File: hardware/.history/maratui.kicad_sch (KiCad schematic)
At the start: 5 parts, among them J1 Power Supply, J2 Lelit Mara, SW1 Button, U1 Ili9341_TFT_320x240

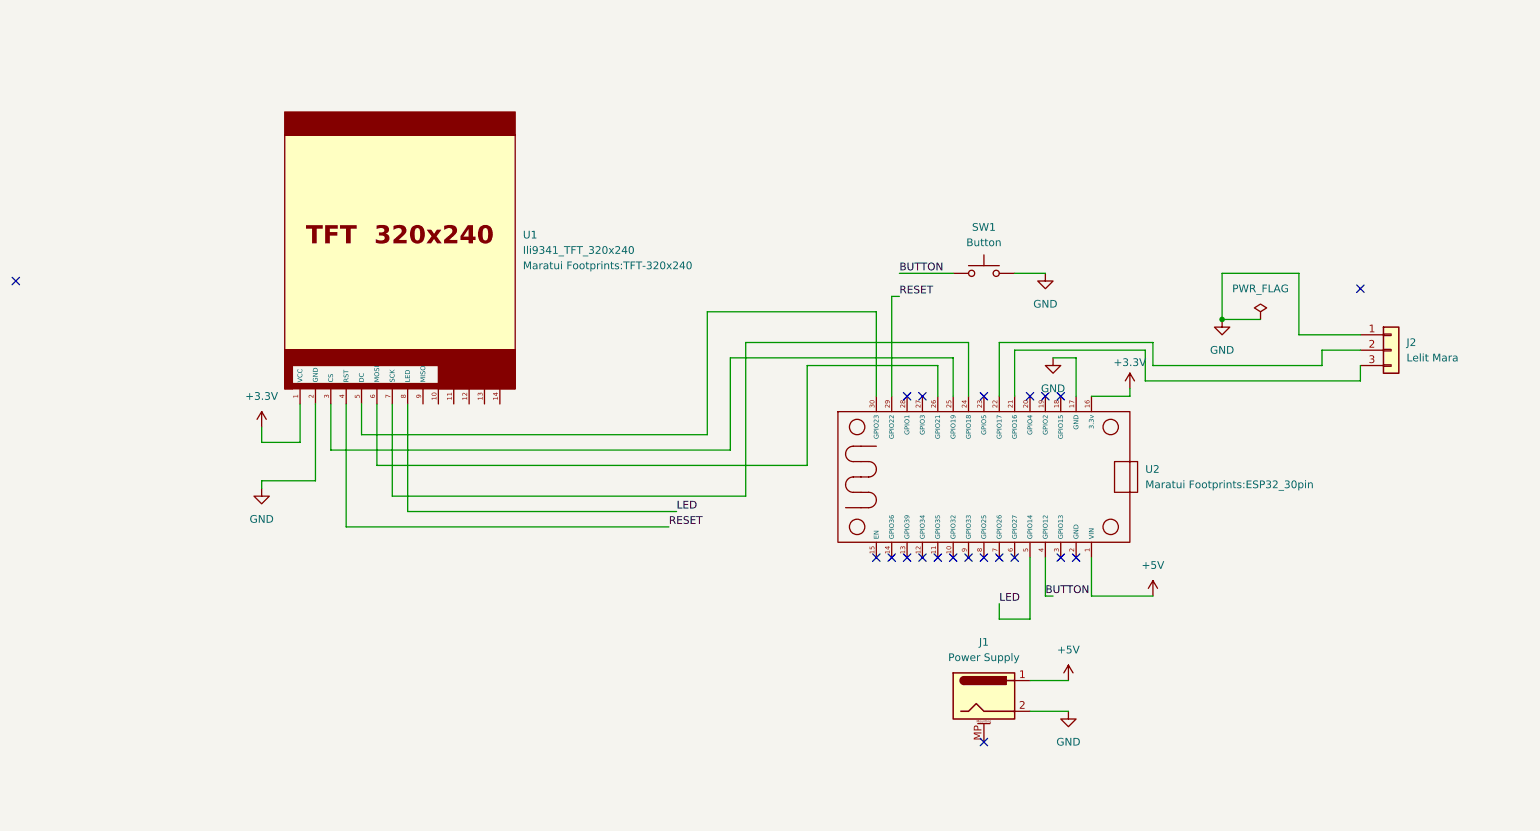
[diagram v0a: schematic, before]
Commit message: feat(hardware): scale-integrated board revision, 3D-printed scale mount
- Replace the board design (schematic, PCB, gerbers, .step) with the
  newer revision that includes the HX711 scale sockets — the previous
  files predated the scale feature entirely and no longer matched the
  firmware.
- Add hardware/lib/footprints/maratui.pretty/HX711_Socket.kicad_mod.
- Add hardware/3d-print/: printable case parts for the dual load-cell
  mount (doppelfuss = double foot, auflage_v2 = scale platform) as
  STEP/STL plus pre-sliced G-code.
- hardware/README.md: HX711 wiring table, 3s-hold calibration note, and
  a 3D-Printed Parts section; drop the stale gerbers/maratui-v1.zip
  reference in favor of the current gerbers.zip (base board) and
  260903_Platine_waage.zip (scale add-on board).

Co-Authored-By: Claude Sonnet 5 <noreply@anthropic.com>
Claude-Session: https://claude.ai/code/session_01Ko6obK5yneSFLNZKCRo7FE
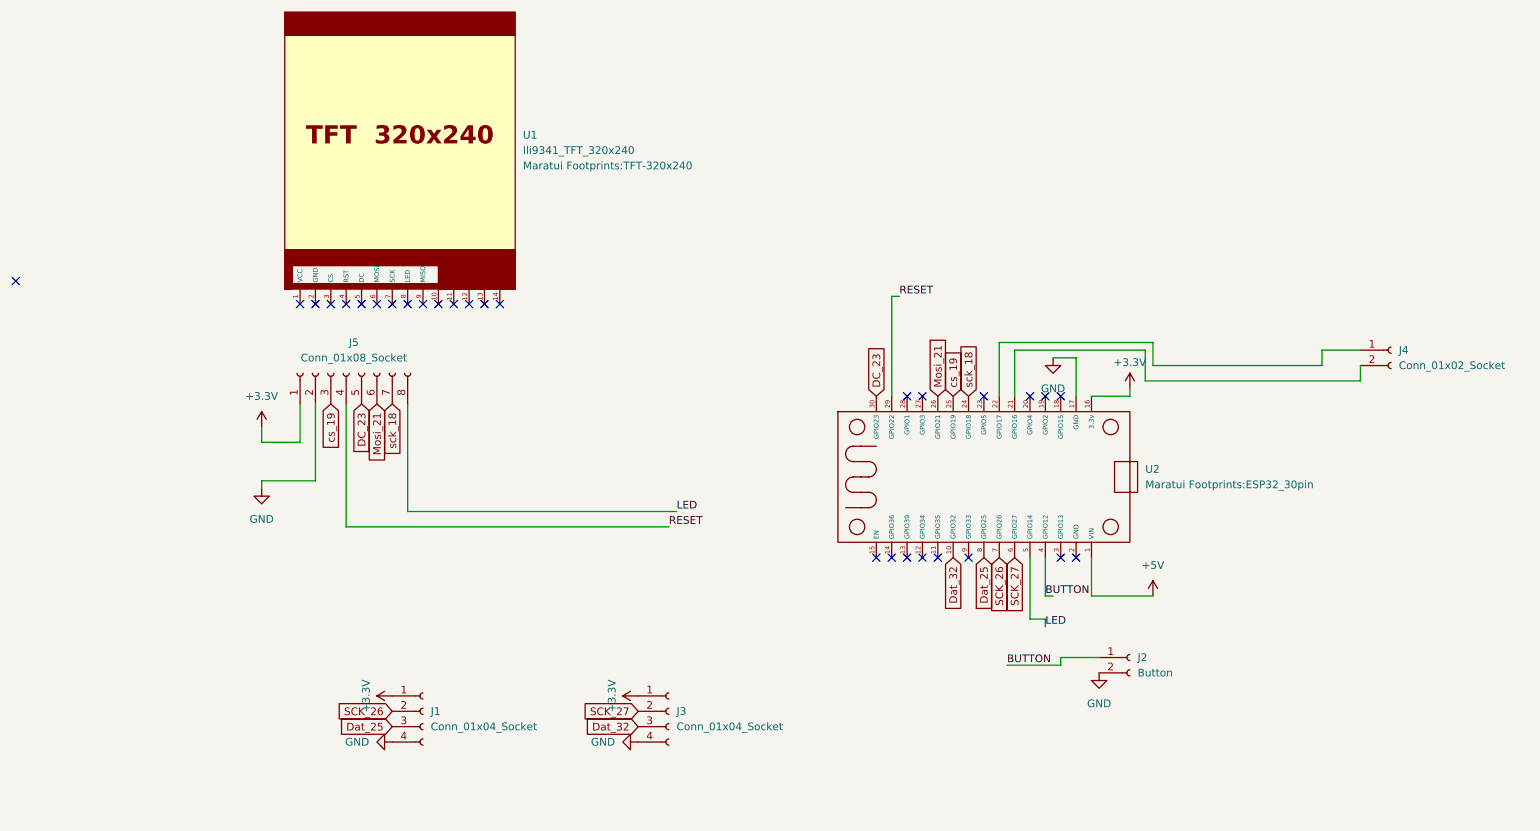
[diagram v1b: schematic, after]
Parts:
- removed J1: Power Supply, Connector_BarrelJack:BarrelJack_CUI_PJ-102AH_Horizontal, symbol Connector:Barrel_Jack_MountingPin
- removed J2: Lelit Mara, Connector_PinHeader_2.54mm:PinHeader_1x03_P2.54mm_Vertical, symbol Connector_Generic:Conn_01x03
- removed SW1: Button, Button_Switch_THT:SW_PUSH_6mm, symbol Switch:SW_Push
- added J1, J3: Conn_01x04_Socket, Connector_PinSocket_2.54mm:PinSocket_1x05_P2.54mm_Vertical, symbol Connector:Conn_01x04_Socket
- added J2: Button, Connector_JST:JST_EH_S2B-EH_1x02_P2.50mm_Horizontal, symbol Connector:Conn_01x02_Socket
- added J4: Conn_01x02_Socket, Connector_JST:JST_EH_S2B-EH_1x02_P2.50mm_Horizontal, symbol Connector:Conn_01x02_Socket
- added J5: Conn_01x08_Socket, Connector_PinSocket_2.54mm:PinSocket_1x08_P2.54mm_Vertical, symbol Connector:Conn_01x08_Socket
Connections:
- net +3.3V: now also J1.1 (Pin_1), J3.1 (Pin_1), J5.1 (Pin_1); no longer U1.1 (VCC)
- net BUTTON: now also J2.1 (Pin_1)
- net GND: now also J1.4 (Pin_4), J2.2 (Pin_2), J3.4 (Pin_4), J5.2 (Pin_2); no longer U1.2 (GND)
- net LED: now also J5.8 (Pin_8); no longer U1.8 (LED)
- net RESET: now also J5.4 (Pin_4); no longer U1.4 (RST)
- net at U1.3 (CS): no longer U2.25 (GPIO19)
- net at U1.5 (DC): no longer U2.30 (GPIO23)
- net at U1.6 (MOSI): no longer U2.26 (GPIO21)
- net at U1.7 (SCK): no longer U2.24 (GPIO18)
- net Dat_32: now reaches U2.10 (GPIO32)
- net Dat_32: now also J3.3 (Pin_3)
- net at U2.21 (GPIO16): now also J4.2 (Pin_2)
- net at U2.22 (GPIO17): now also J4.1 (Pin_1)
- net SCK_27: now reaches U2.6 (GPIO27)
- net SCK_27: now also J3.2 (Pin_2)
- net SCK_26: now reaches U2.7 (GPIO26)
- net SCK_26: now also J1.2 (Pin_2)
- net Dat_25: now reaches U2.8 (GPIO25)
- net Dat_25: now also J1.3 (Pin_3)
- new net DC_23: J5.5 (Pin_5), U2.30 (GPIO23)
- new net Mosi_21: J5.6 (Pin_6), U2.26 (GPIO21)
- new net cs_19: J5.3 (Pin_3), U2.25 (GPIO19)
- new net sck_18: J5.7 (Pin_7), U2.24 (GPIO18)
- no-connect marks 21 -> 29
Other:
- moved on the sheet: U1

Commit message: hardware: update PCB and gerbers for the ordered board revision
Updated schematic/PCB and regenerated gerbers.zip for the board
revision that was ordered from fab. Removed the now-superseded
separate scale add-on gerber zip (260903_Platine_waage.zip) — the
scale cells are part of the single-board gerbers.zip export.

Co-Authored-By: Claude Sonnet 5 <noreply@anthropic.com>
Claude-Session: https://claude.ai/code/session_01Ko6obK5yneSFLNZKCRo7FE
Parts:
- J2, J4: footprint Connector_JST:JST_EH_S2B-EH_1x02_P2.50mm_Horizontal -> Connector_JST:JST_EH_B2B-EH-A_1x02_P2.50mm_Vertical
- J5: footprint Connector_PinSocket_2.54mm:PinSocket_1x08_P2.54mm_Vertical -> Connector_PinSocket_2.54mm:PinSocket_1x14_P2.54mm_Vertical
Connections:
- no-connect marks 29 -> 28
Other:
- moved on the sheet: J1, J3
